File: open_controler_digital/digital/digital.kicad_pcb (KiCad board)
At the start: 2 copper layers, 79 parts, among them J1 d_o_01x10, J2 d_i_01x10, J3 Conn_02x20_Odd_Even, J4 Conn_01x02, Q1 BC856, Q10 VP0610T, Q11 VP0610T, Q12 VP0610T, Q2 BC856, Q3 VP0610T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

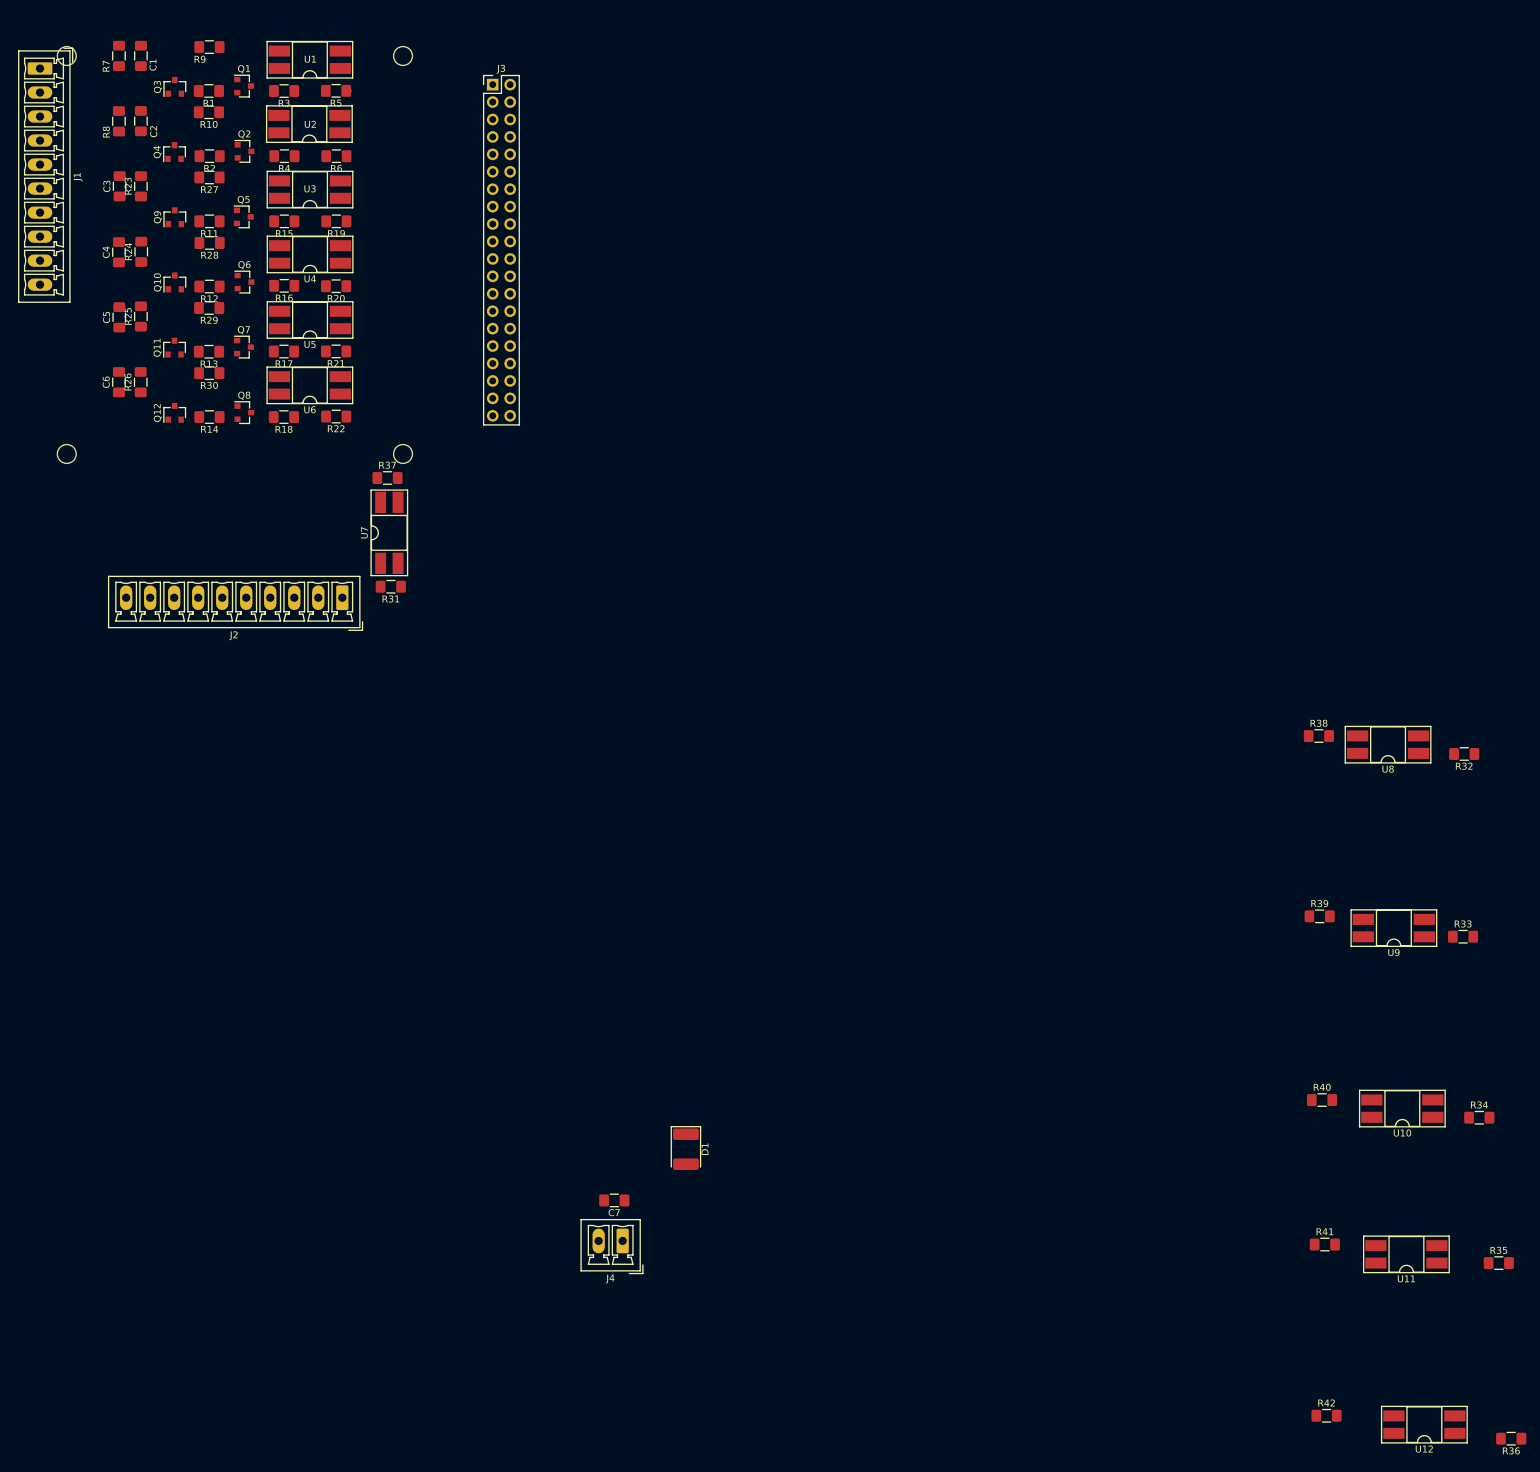
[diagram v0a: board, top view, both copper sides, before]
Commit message: desarrollo de la PCB con la huella de la Raspberry
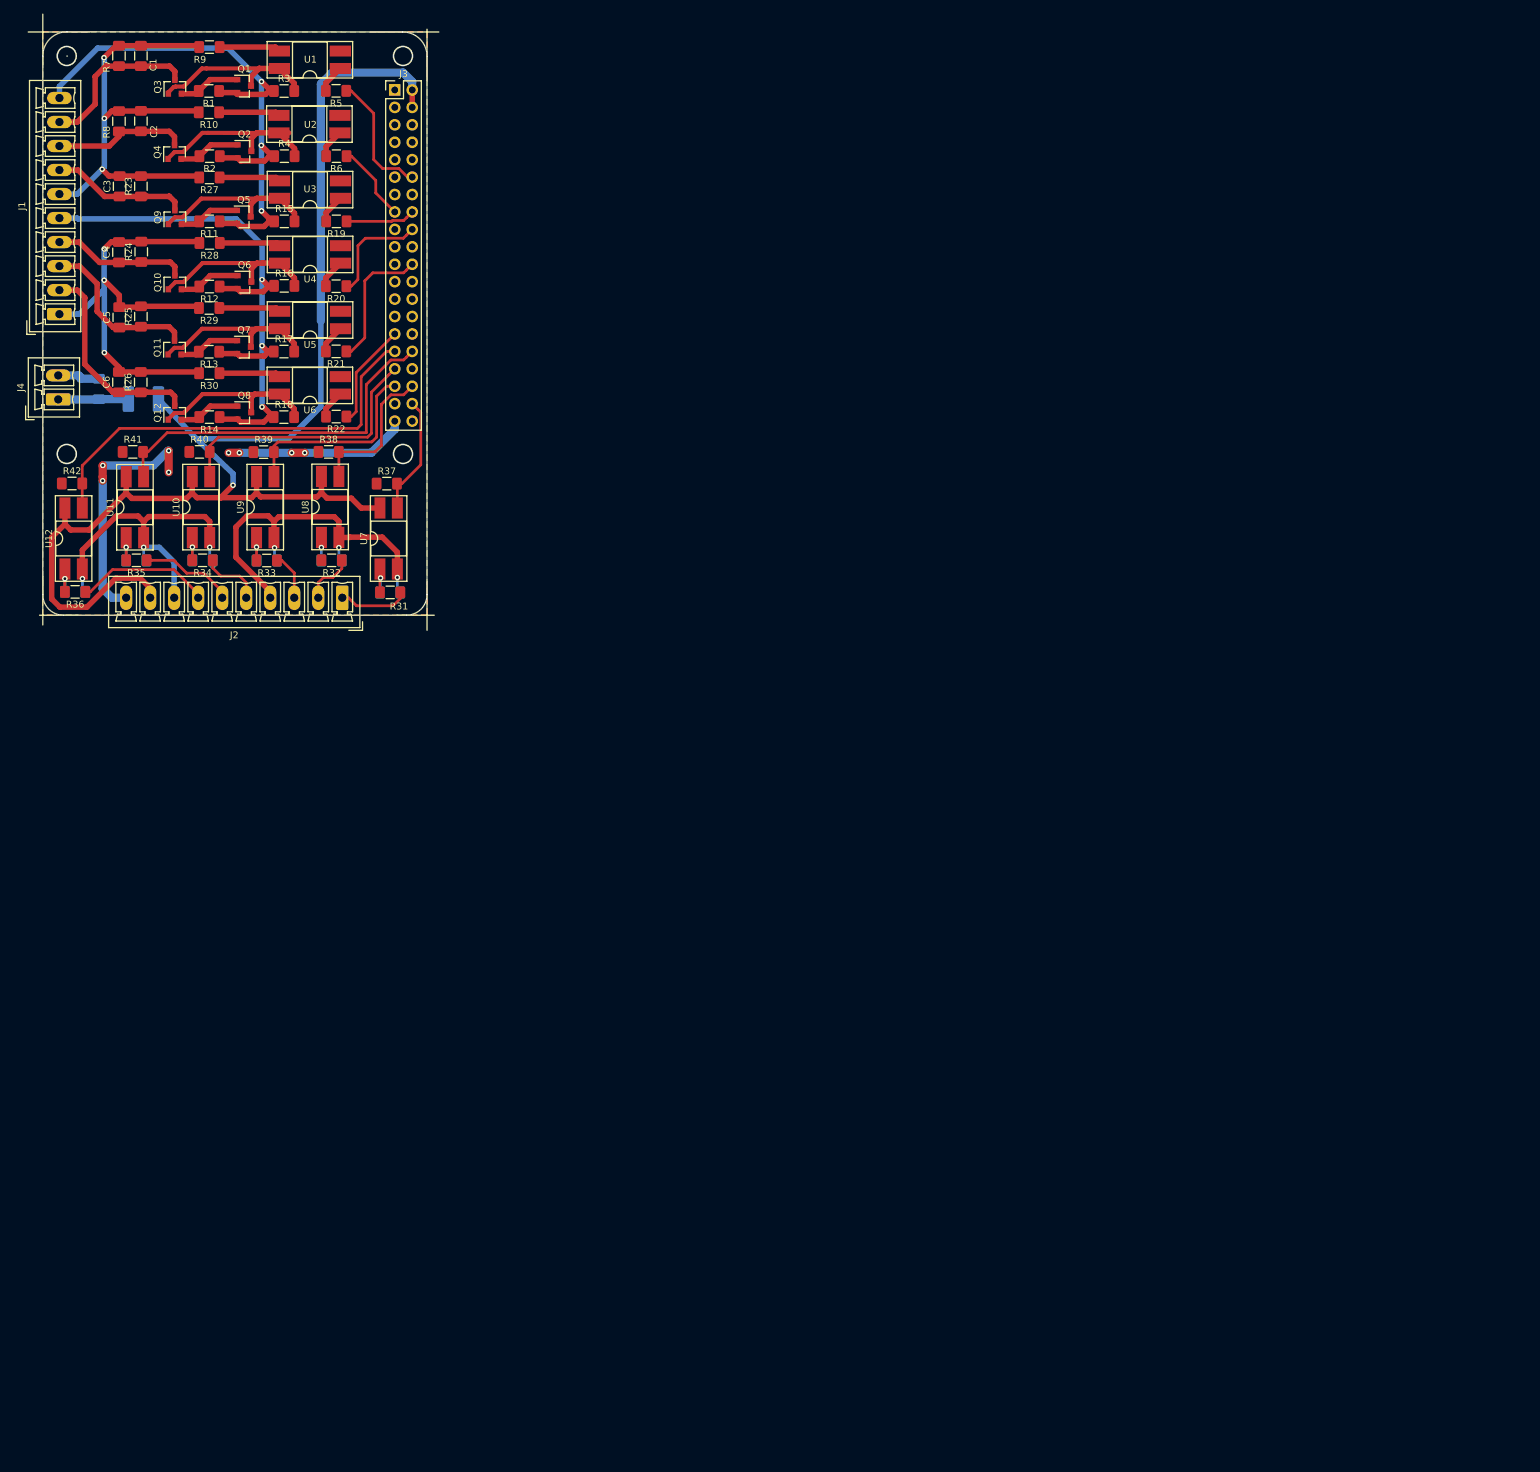
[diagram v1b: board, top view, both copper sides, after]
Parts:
- added C10: 10, Capacitor_SMD:C_1206_3216Metric_Pad1.42x1.75mm_HandSolder, B.Cu at (105.9, 118.7)
- added C11: 10, Capacitor_SMD:C_1206_3216Metric_Pad1.42x1.75mm_HandSolder, B.Cu at (96.6, 118.7)
- added C12: 10, Capacitor_SMD:C_1206_3216Metric_Pad1.42x1.75mm_HandSolder, B.Cu at (86.9, 118.7)
- added C13: 10, Capacitor_SMD:C_1206_3216Metric_Pad1.42x1.75mm_HandSolder, B.Cu at (78.0, 123.3)
- added C8: 10, Capacitor_SMD:C_1206_3216Metric_Pad1.42x1.75mm_HandSolder, B.Cu at (123.9, 123.4)
- added C9: 10, Capacitor_SMD:C_1206_3216Metric_Pad1.42x1.75mm_HandSolder, B.Cu at (115.4, 118.7)
- C7, D1: moved to B.Cu
- moved R36 243.0 mm to (78.0, 123.3)
- moved U12 235.4 mm to (77.8, 115.5), turned to 90 degrees
- moved R42 227.8 mm to (77.5, 107.5)
- moved R35 223.4 mm to (86.9, 118.7), turned to 180 degrees
- moved U11 214.9 mm to (86.7, 111.0), turned to 90 degrees
- moved R41 208.6 mm to (86.4, 102.9)
- moved R34 203.0 mm to (96.6, 118.7), turned to 180 degrees
- moved U10 195.8 mm to (96.3, 110.9), turned to 90 degrees
- moved R40 188.9 mm to (96.1, 102.9)
- moved R33 182.8 mm to (105.9, 118.7), turned to 180 degrees
- moved U9 175.6 mm to (105.7, 110.9), turned to 90 degrees
- moved R39 168.1 mm to (105.5, 102.9)
- moved R32 167.5 mm to (115.4, 118.7)
- moved U8 158.0 mm to (115.2, 110.9), turned to 90 degrees
- moved R38 150.1 mm to (114.9, 102.9)
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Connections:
- C7 pad 1: 5v_1 -> 5v
- J1 pad 1: vo0 -> go1
- J1 pad 10: go1 -> vo0
- J1 pad 2: do00 -> do12
- J1 pad 3: do01 -> do11
- J1 pad 4: do02 -> do10
- J1 pad 5: go0 -> vo1
- J1 pad 6: vo1 -> go0
- J1 pad 7: do10 -> do02
- J1 pad 8: do11 -> do01
- J1 pad 9: do12 -> do00
- J3 pad 1: 5v_1 -> Net-(J3-Pad1)
- J3 pad 10: GND_1 -> Net-(J3-Pad10)
- J3 pad 11: GPIO_18 -> Net-(J3-Pad11)
- J3 pad 12: Net-(J3-Pad12) -> GPIO_18
- J3 pad 13: GND_1 -> Net-(J3-Pad13)
- J3 pad 14: Net-(J3-Pad14) -> GND_1
- J3 pad 15: GPIO_23 -> GPIO_22
- J3 pad 16: GPIO_22 -> GPIO_23
- J3 pad 17: GPIO_24 -> Net-(J3-Pad17)
- J3 pad 18: Net-(J3-Pad18) -> GPIO_24
- J3 pad 19: GND_1 -> Net-(J3-Pad19)
- J3 pad 2: Net-(J3-Pad2) -> 5v_1
- J3 pad 20: Net-(J3-Pad20) -> GND_1
- J3 pad 21: GPIO_25 -> Net-(J3-Pad21)
- J3 pad 22: Net-(J3-Pad22) -> GPIO_25
- J3 pad 25: Net-(J3-Pad25) -> GND_1
- J3 pad 26: GND_1 -> Net-(J3-Pad26)
- J3 pad 29: GND_1 -> GPIO_5
- J3 pad 3: 5v_1 -> Net-(J3-Pad3)
- J3 pad 30: GPIO_5 -> GND_1
- J3 pad 31: GPIO_12 -> GPIO_6
- J3 pad 32: GPIO_6 -> GPIO_12
- J3 pad 33: GND_1 -> GPIO_13
- J3 pad 34: GPIO_13 -> GND_1
- J3 pad 35: GPIO_16 -> GPIO_19
- J3 pad 36: GPIO_19 -> GPIO_16
- J3 pad 37: GPIO_20 -> Net-(J3-Pad37)
- J3 pad 38: Net-(J3-Pad38) -> GPIO_20
- J3 pad 39: Net-(J3-Pad39) -> GND_1
- J3 pad 4: Net-(J3-Pad4) -> 5v_1
- J3 pad 40: GND_1 -> Net-(J3-Pad40)
- J3 pad 5: GND_1 -> Net-(J3-Pad5)
- J3 pad 6: Net-(J3-Pad6) -> GND_1
- J3 pad 9: Net-(J3-Pad9) -> GND_1
- R37 pad 2: GPIO_6 -> GPIO_20
- R38 pad 2: GPIO_12 -> GPIO_16
- R39 pad 2: GPIO_13 -> GPIO_19
- R40 pad 2: GPIO_19 -> GPIO_13
- R41 pad 2: GPIO_16 -> GPIO_12
- R42 pad 2: GPIO_20 -> GPIO_6
- U10 pad 3: GPIO_19 -> GPIO_13
- U11 pad 3: GPIO_16 -> GPIO_12
- U12 pad 3: GPIO_20 -> GPIO_6
- U7 pad 3: GPIO_6 -> GPIO_20
- U8 pad 3: GPIO_12 -> GPIO_16
- U9 pad 3: GPIO_13 -> GPIO_19
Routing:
- net 5v_1: track 0.00 -> 198.3 mm, vias 0 -> 1
- net vo1: track 0.00 -> 86.9 mm, vias 0 -> 3
- net vo0: track 0.00 -> 86.4 mm, vias 0 -> 3
- net go1: track 0.00 -> 71.1 mm, vias 0 -> 3
- net GND_1: track 0.00 -> 68.7 mm, vias 0 -> 8
- net go0: track 0.00 -> 67.8 mm, vias 0 -> 3
- net GPIO_6: track 0.00 -> 63.4 mm
- net gi2: track 0.00 -> 56.9 mm, vias 0 -> 3
- net GPIO_12: track 0.00 -> 53.1 mm
- net gi3: track 0.00 -> 51.0 mm, vias 0 -> 3
- net GPIO_13: track 0.00 -> 39.6 mm
- net do12: track 0.00 -> 30.3 mm
- net GPIO_19: track 0.00 -> 29.2 mm
- net Net-(Q2-Pad3): track 0.00 -> 26.6 mm
- net Net-(Q10-Pad1): track 0.00 -> 26.0 mm
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- added copper zone on B.Cu, net GND_1
- added copper zone on F.Cu, net GND_1
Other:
- board outline added: 56 x 85 mm

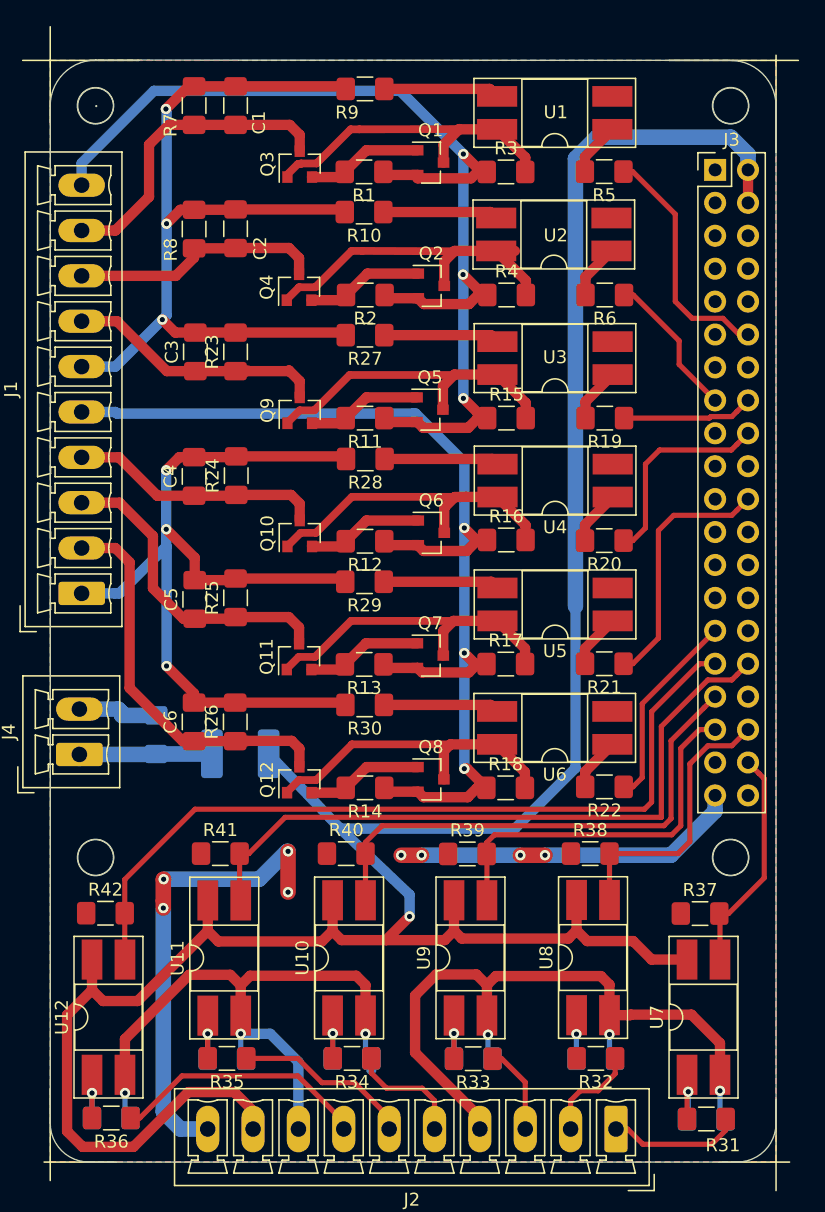
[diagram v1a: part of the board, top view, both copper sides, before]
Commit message: version de hw operativa
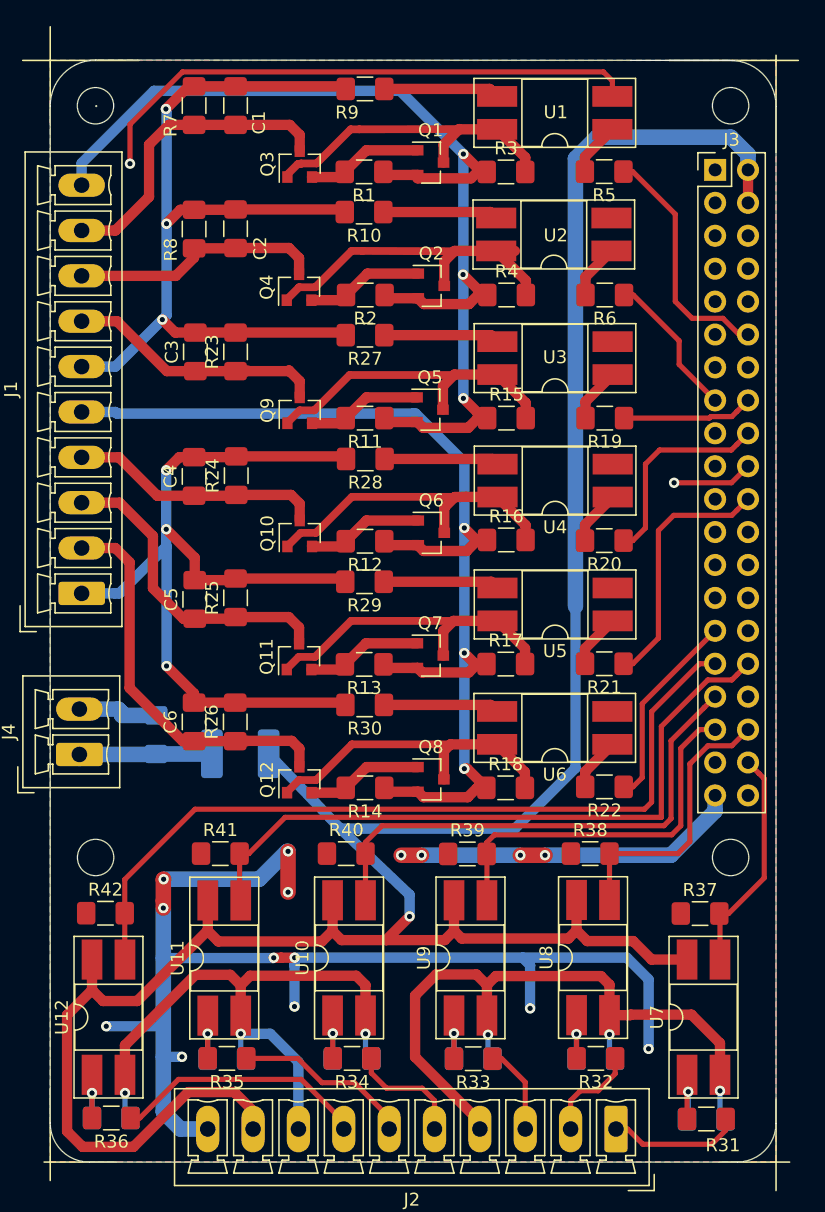
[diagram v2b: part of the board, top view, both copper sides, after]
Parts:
- removed RP?: Raspberry_Pi_2_3, Raspberry-Pi-4-library-for-kicad:raspberrypi_2_3
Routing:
- net GND_1: track 68.7 -> 175.6 mm, vias 8 -> 17
- net Net-(C9-Pad1): track 3.36 -> 6.70 mm
- net gi3: track 51.0 -> 49.9 mm

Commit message: version para fabricacion
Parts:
- C1, C2, C3, C4, C5, C6, C7: value C -> 10
- Q10, Q11, Q12, Q3, Q4, Q9: value VP0610T -> JM
